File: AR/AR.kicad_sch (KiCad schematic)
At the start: 16 parts

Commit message: Update AR design
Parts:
- R?: value 4.7k -> 1k
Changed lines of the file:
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@@
       (effects (font (size 1.27 1.27)) (justify left))
     )
-    (property "Value" "4.7k" (id 1) (at 135.89 90.17 0)
+    (property "Value" "1k" (id 1) (at 135.89 90.17 0)
       (effects (font (size 1.27 1.27)) (justify left))
     )
@@
     )
     (path "/7359da98-671d-480a-b466-89bbe372ba77"
-      (reference "R?") (unit 1) (value "4.7k") (footprint "Resistor_THT:R_Axial_DIN0207_L6.3mm_D2.5mm_P7.62mm_Horizontal")
+      (reference "R?") (unit 1) (value "1k") (footprint "Resistor_THT:R_Axial_DIN0207_L6.3mm_D2.5mm_P7.62mm_Horizontal")
     )
     (path "/9c2439e7-5ae1-4a7e-8076-4baa2ba55933"

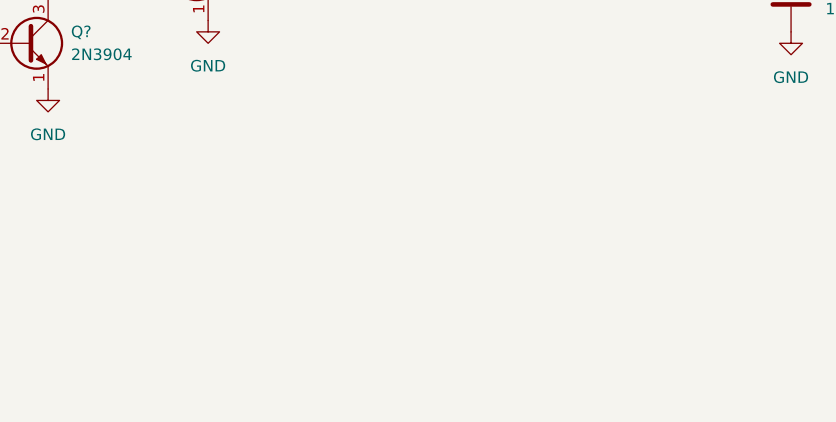
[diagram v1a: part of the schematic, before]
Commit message: Update power connectors
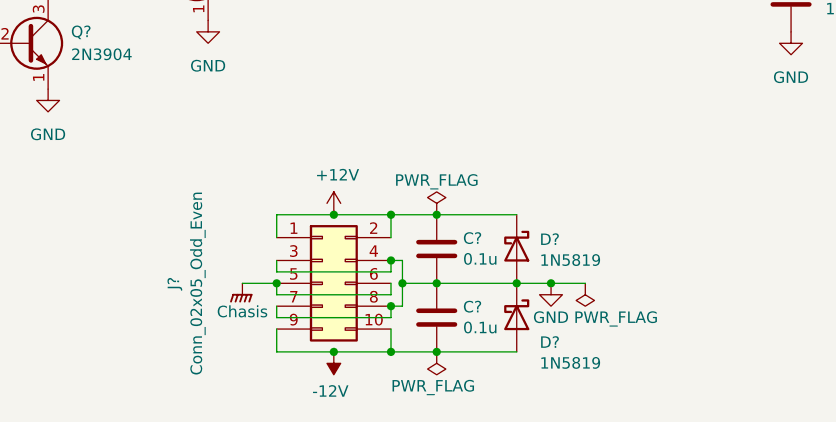
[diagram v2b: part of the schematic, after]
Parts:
- added C? (x2): 0.1u, Capacitor_THT:C_Disc_D5.0mm_W2.5mm_P5.00mm, symbol Device:C
- added D? (x2): 1N5819, Diode_THT:D_DO-41_SOD81_P10.16mm_Horizontal, symbol Diode:1N5819
- added J?: Conn_02x05_Odd_Even, Connector_PinHeader_2.54mm:PinHeader_2x05_P2.54mm_Vertical, symbol Connector_Generic:Conn_02x05_Odd_Even
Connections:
- net +12V: now also C?.1, D?.1 (K), J?.1 (Pin_1), J?.2 (Pin_2)
- net GND: now also C?.1, C?.2, D?.1 (K), D?.2 (A), J?.3 (Pin_3), J?.4 (Pin_4), J?.7 (Pin_7), J?.8 (Pin_8)
- new net -12V: C?.2, D?.2 (A), J?.10 (Pin_10), J?.9 (Pin_9)
- new net Chasis: J?.5 (Pin_5), J?.6 (Pin_6)
